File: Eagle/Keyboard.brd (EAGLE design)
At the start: 100 x 80 mm, 104 parts

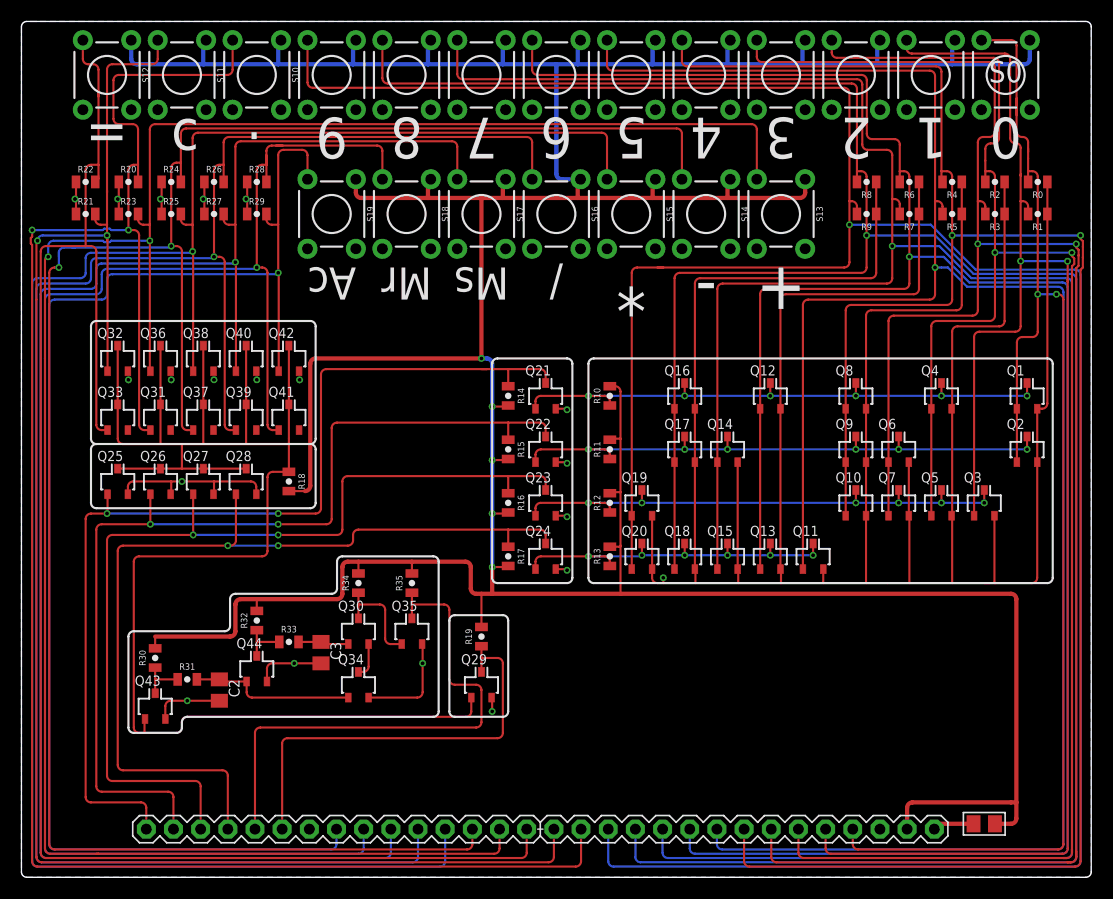
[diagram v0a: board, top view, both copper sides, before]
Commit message: Silk cleanup. Routing of GND instead of floodfill
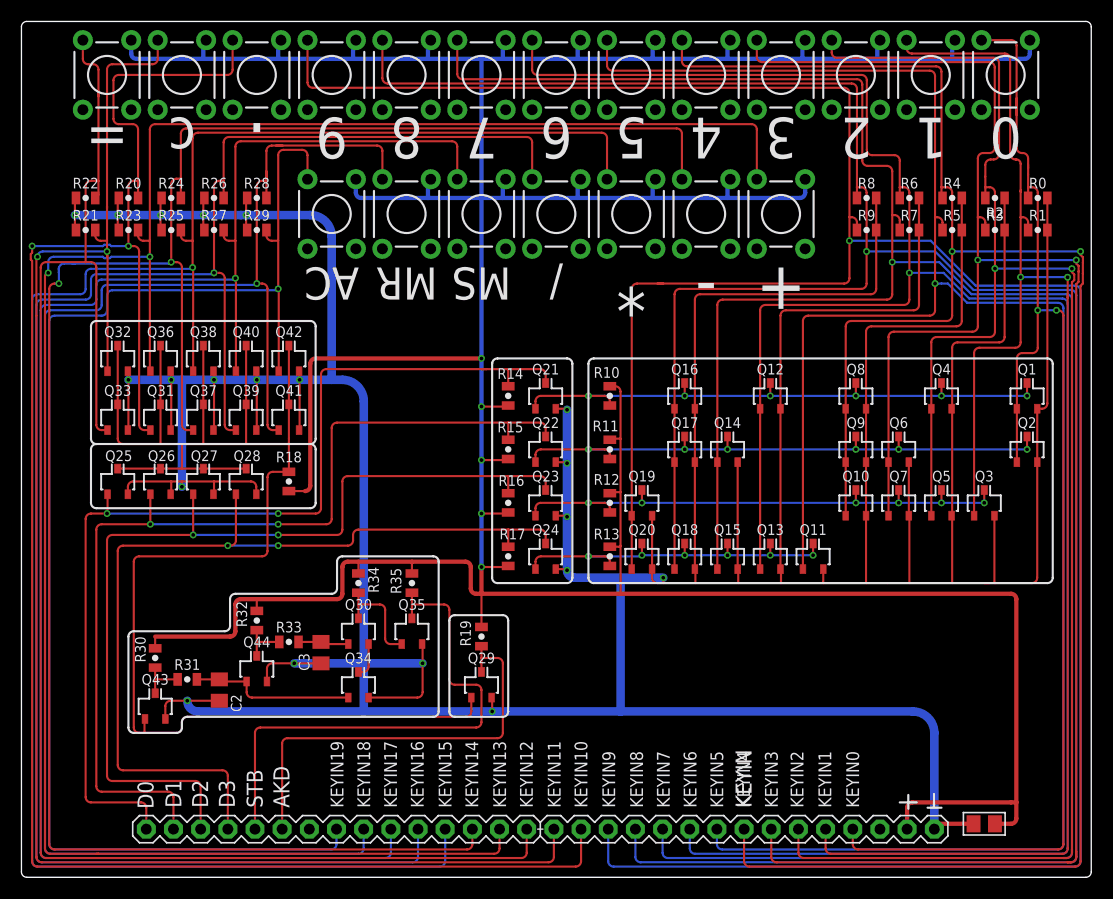
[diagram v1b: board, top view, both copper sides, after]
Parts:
- moved R0 1.50 mm to (95.0, 63.5)
- moved R1 1.50 mm to (95.0, 60.5)
- moved R2 1.50 mm to (91.0, 63.5)
- moved R20 1.50 mm to (10.0, 63.5)
- moved R21 1.50 mm to (6.00, 60.5)
- moved R22 1.50 mm to (6.00, 63.5)
- moved R23 1.50 mm to (10.0, 60.5)
- moved R24 1.50 mm to (14.0, 63.5)
- moved R25 1.50 mm to (14.0, 60.5)
- moved R26 1.50 mm to (18.0, 63.5)
- moved R27 1.50 mm to (18.0, 60.5)
- moved R28 1.50 mm to (22.0, 63.5)
- moved R29 1.50 mm to (22.0, 60.5)
- moved R3 1.50 mm to (91.0, 60.5)
- moved R4 1.50 mm to (87.0, 63.5)
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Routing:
- net GND: track 367.0 -> 617.9 mm
- net VCC: track 409.8 -> 406.9 mm
- net KEYIN8: track 231.7 -> 230.2 mm
- net KEYIN3: track 175.6 -> 174.1 mm
- net KEYIN9: track 247.5 -> 246.0 mm
- net KEYIN7: track 219.0 -> 217.5 mm
- net KEYIN6: track 203.6 -> 202.1 mm
- net KEYIN5: track 191.7 -> 190.2 mm
- net KEYIN4: track 184.8 -> 183.3 mm
- net KEYIN2: track 160.7 -> 159.2 mm
- net KEYIN19: track 130.1 -> 128.6 mm
- net KEYIN18: track 150.3 -> 148.8 mm
- net KEYIN17: track 155.0 -> 153.5 mm
- net KEYIN16: track 173.7 -> 172.2 mm
- net KEYIN15: track 179.8 -> 178.3 mm
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- removed copper zone on layer 16, net GND
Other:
- board text added: "AC"
- board text added: "AKD"
- board text added: "D0"
- board text added: "D1"
- board text added: "D2"
- board text added: "D3"
- board text added: "KEYIN"
- board text added: "KEYIN0"
- board text added: "KEYIN1"
- board text added: "KEYIN10"
- board text added: "KEYIN11"
- board text added: "KEYIN12"
- board text added: "KEYIN13"
- board text added: "KEYIN14"
- board text added: "KEYIN15"
- board text added: "KEYIN16"
- board text added: "KEYIN17"
- board text added: "KEYIN18"
- board text added: "KEYIN19"
- board text added: "KEYIN2"
- board text added: "KEYIN3"
- board text added: "KEYIN4"
- board text added: "KEYIN5"
- board text added: "KEYIN6"
- board text added: "KEYIN7"
- board text added: "KEYIN8"
- board text added: "KEYIN9"
- board text added: "Keyboard decoder Rev1"
- board text added: "MR"
- board text added: "MS"
- board text added: "STB"
- board text added: "SmallRoomLabs"
- board text removed: "Ac"
- board text removed: "Mr"
- board text removed: "Ms"
